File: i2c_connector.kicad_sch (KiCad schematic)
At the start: 5 parts, among them J3 SM04B-SRSS-TB(LF)(SN)

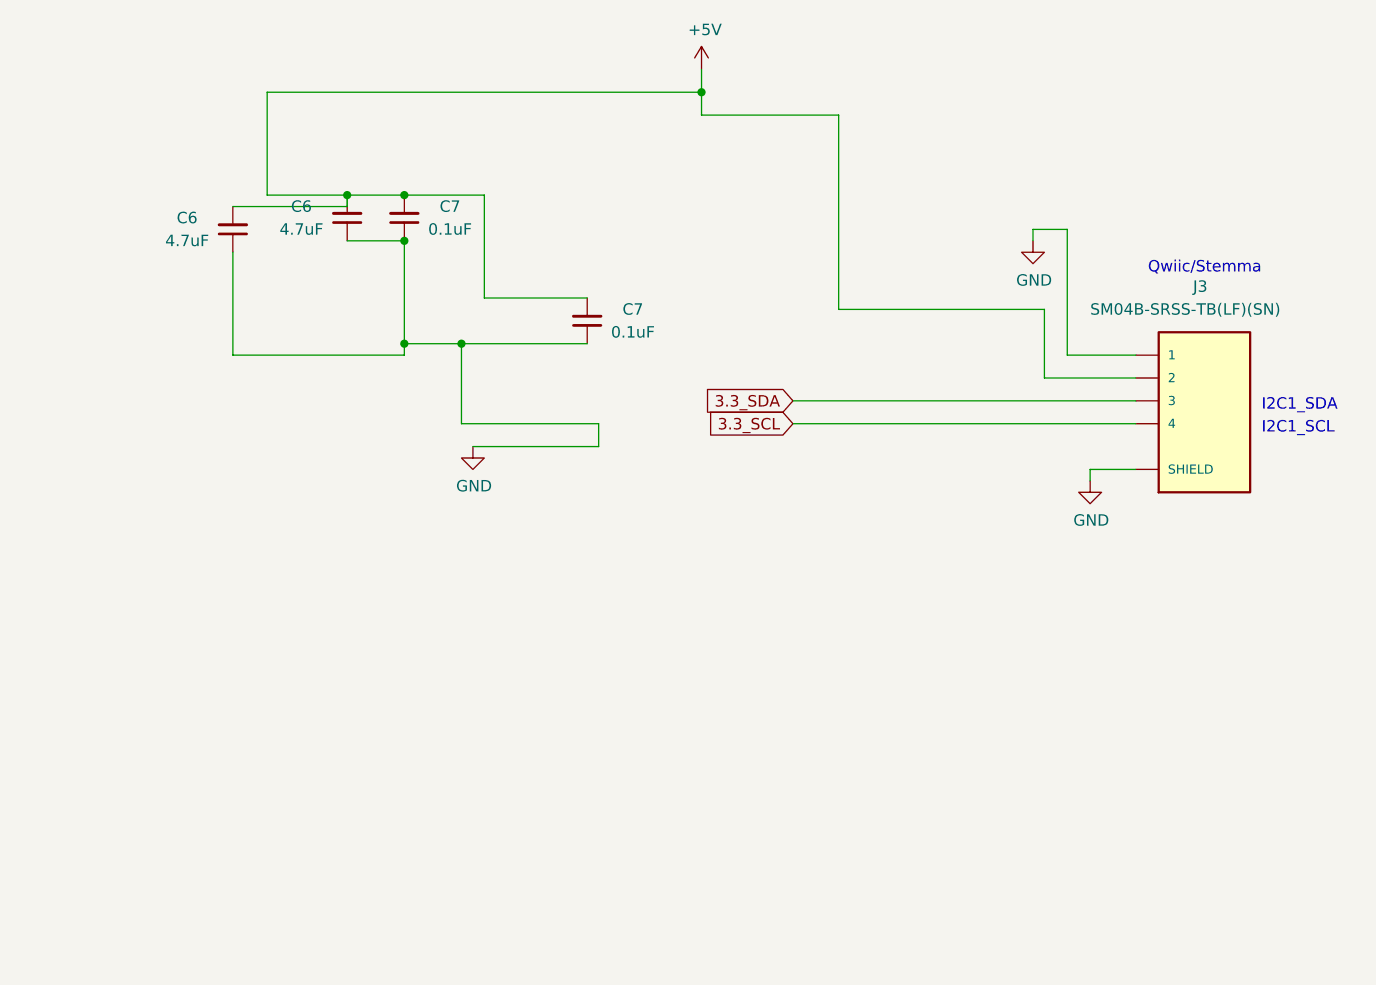
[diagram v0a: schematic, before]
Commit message: Add testpoints
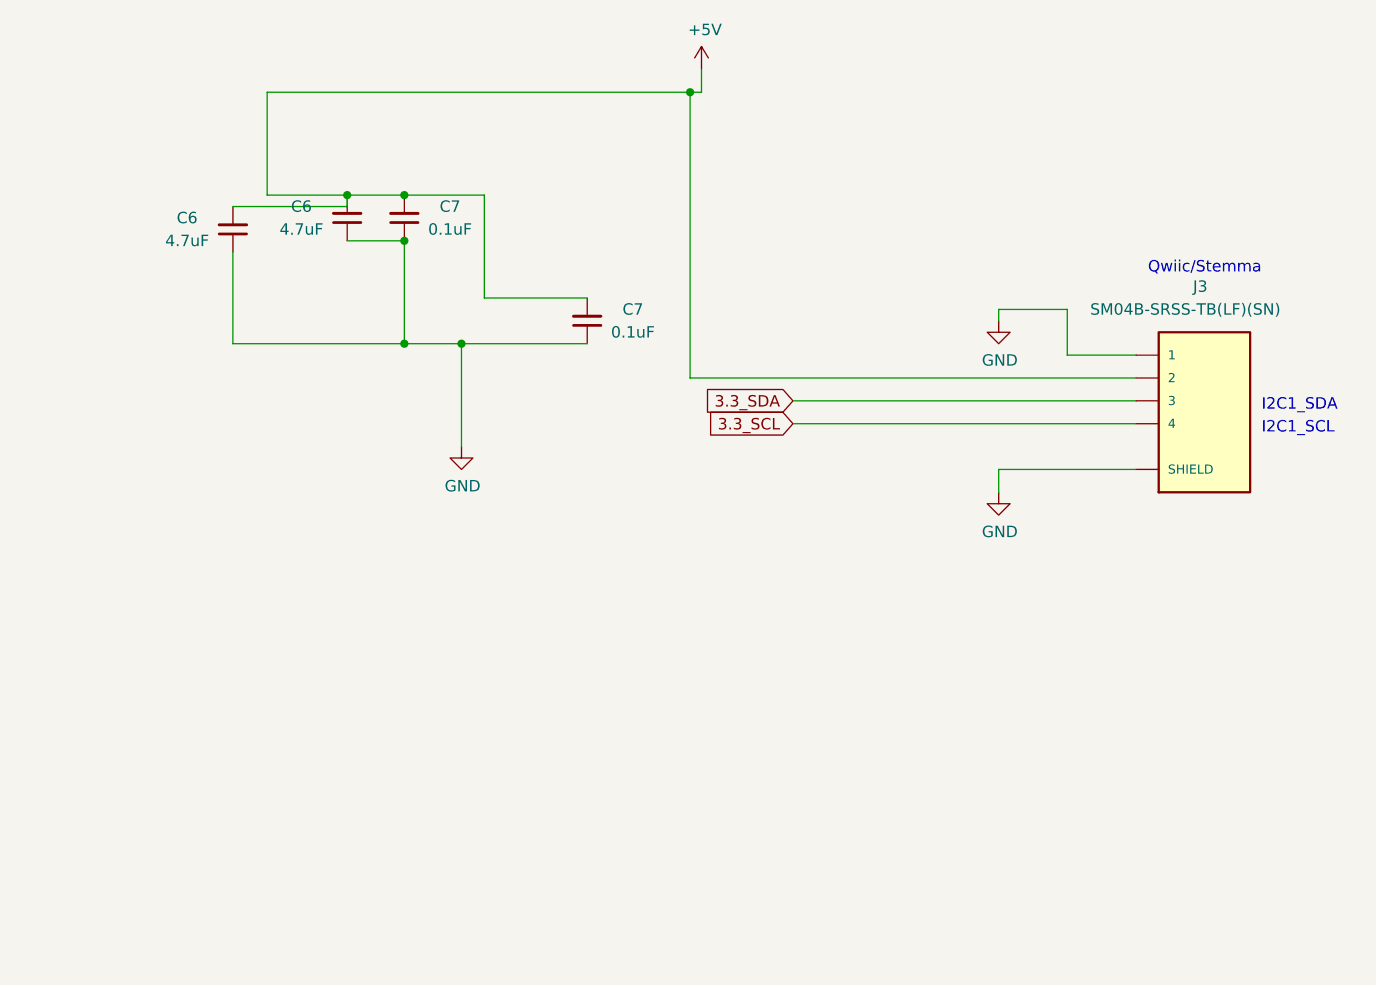
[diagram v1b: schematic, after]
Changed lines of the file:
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@@
   (junction (at 96.52 92.71) (diameter 0) (color 0 0 0 0)
   )
+  (junction (at 128.27 64.77) (diameter 0) (color 0 0 0 0)
+  )
   (junction (at 102.87 92.71) (diameter 0) (color 0 0 0 0)
   )
@@
   (junction (at 90.17 76.2) (diameter 0) (color 0 0 0 0)
   )
-  (junction (at 129.54 64.77) (diameter 0) (color 0 0 0 0)
-  )
-  (wire (pts (xy 172.72 106.68) (xy 172.72 107.95))
-    (stroke (width 0) (type default))
-  )
-  (wire (pts (xy 166.37 81.28) (xy 166.37 80.01))
+  (wire (pts (xy 162.56 106.68) (xy 162.56 109.22))
+    (stroke (width 0) (type default))
+  )
+  (wire (pts (xy 162.56 90.17) (xy 162.56 88.9))
     (stroke (width 0) (type solid))
   )
@@
     (stroke (width 0) (type default))
   )
-  (wire (pts (xy 102.87 92.71) (xy 102.87 101.6))
-    (stroke (width 0) (type default))
-  )
-  (wire (pts (xy 77.47 93.98) (xy 77.47 82.55))
-    (stroke (width 0) (type default))
-  )
-  (wire (pts (xy 96.52 93.98) (xy 96.52 92.71))
-    (stroke (width 0) (type default))
-  )
-  (wire (pts (xy 118.11 101.6) (xy 118.11 104.14))
+  (wire (pts (xy 77.47 92.71) (xy 77.47 82.55))
+    (stroke (width 0) (type default))
+  )
+  (wire (pts (xy 102.87 92.71) (xy 102.87 104.14))
     (stroke (width 0) (type default))
   )
@@
     (stroke (width 0) (type default))
   )
-  (wire (pts (xy 167.64 96.52) (xy 167.64 88.9))
-    (stroke (width 0) (type solid))
-  )
   (wire (pts (xy 139.7 101.6) (xy 177.8 101.6))
     (stroke (width 0) (type solid))
@@
     (stroke (width 0) (type default))
   )
-  (wire (pts (xy 77.47 93.98) (xy 96.52 93.98))
+  (wire (pts (xy 77.47 92.71) (xy 96.52 92.71))
     (stroke (width 0) (type default))
   )
@@
     (stroke (width 0) (type default))
   )
-  (wire (pts (xy 170.18 80.01) (xy 170.18 93.98))
-    (stroke (width 0) (type solid))
-  )
-  (wire (pts (xy 144.78 67.31) (xy 129.54 67.31))
-    (stroke (width 0) (type default))
-  )
-  (wire (pts (xy 102.87 101.6) (xy 118.11 101.6))
+  (wire (pts (xy 170.18 88.9) (xy 170.18 93.98))
+    (stroke (width 0) (type solid))
+  )
+  (wire (pts (xy 128.27 96.52) (xy 177.8 96.52))
     (stroke (width 0) (type default))
   )
@@
     (stroke (width 0) (type default))
   )
-  (wire (pts (xy 118.11 104.14) (xy 104.14 104.14))
-    (stroke (width 0) (type default))
-  )
   (wire (pts (xy 105.41 87.63) (xy 116.84 87.63))
     (stroke (width 0) (type default))
@@
     (stroke (width 0) (type default))
   )
-  (wire (pts (xy 81.28 64.77) (xy 129.54 64.77))
+  (wire (pts (xy 81.28 64.77) (xy 128.27 64.77))
     (stroke (width 0) (type default))
   )
@@
     (stroke (width 0) (type solid))
   )
-  (wire (pts (xy 129.54 64.77) (xy 129.54 67.31))
-    (stroke (width 0) (type default))
-  )
-  (wire (pts (xy 177.8 96.52) (xy 167.64 96.52))
-    (stroke (width 0) (type solid))
-  )
-  (wire (pts (xy 144.78 67.31) (xy 144.78 88.9))
-    (stroke (width 0) (type default))
-  )
-  (wire (pts (xy 177.8 106.68) (xy 172.72 106.68))
+  (wire (pts (xy 128.27 64.77) (xy 129.54 64.77))
+    (stroke (width 0) (type default))
+  )
+  (wire (pts (xy 128.27 64.77) (xy 128.27 96.52))
+    (stroke (width 0) (type default))
+  )
+  (wire (pts (xy 177.8 106.68) (xy 162.56 106.68))
     (stroke (width 0) (type default))
   )
@@
     (stroke (width 0) (type default))
   )
-  (wire (pts (xy 166.37 80.01) (xy 170.18 80.01))
+  (wire (pts (xy 162.56 88.9) (xy 170.18 88.9))
     (stroke (width 0) (type solid))
   )
@@
   )
   (wire (pts (xy 139.7 99.06) (xy 177.8 99.06))
-    (stroke (width 0) (type solid))
-  )
-  (wire (pts (xy 144.78 88.9) (xy 167.64 88.9))
     (stroke (width 0) (type solid))
   )
@@
     )
   )
-  (symbol (lib_id "power:GND") (at 166.37 81.28 0) (unit 1)
-    (in_bom yes) (on_board yes) (dnp no)
-    (property "Reference" "#PWR0109" (at 166.37 87.63 0)
-      (effects (font (size 1.27 1.27)) hide)
-    )
-    (property "Value" "GND" (at 166.497 85.6742 0)
-      (effects (font (size 1.27 1.27)))
-    )
-    (property "Footprint" "" (at 166.37 81.28 0)
-      (effects (font (size 1.27 1.27)) hide)
-    )
-    (property "Datasheet" "" (at 166.37 81.28 0)
+  (symbol (lib_id "power:GND") (at 162.56 90.17 0) (unit 1)
+    (in_bom yes) (on_board yes) (dnp no)
+    (property "Reference" "#PWR0109" (at 162.56 96.52 0)
+      (effects (font (size 1.27 1.27)) hide)
+    )
+    (property "Value" "GND" (at 162.687 94.5642 0)
+      (effects (font (size 1.27 1.27)))
+    )
+    (property "Footprint" "" (at 162.56 90.17 0)
+      (effects (font (size 1.27 1.27)) hide)
+    )
+    (property "Datasheet" "" (at 162.56 90.17 0)
       (effects (font (size 1.27 1.27)) hide)
     )
@@
     )
   )
-  (symbol (lib_id "power:GND") (at 104.14 104.14 0) (unit 1)
-    (in_bom yes) (on_board yes) (dnp no)
-    (property "Reference" "#PWR033" (at 104.14 110.49 0)
-      (effects (font (size 1.27 1.27)) hide)
-    )
-    (property "Value" "GND" (at 104.267 108.5342 0)
-      (effects (font (size 1.27 1.27)))
-    )
-    (property "Footprint" "" (at 104.14 104.14 0)
-      (effects (font (size 1.27 1.27)) hide)
-    )
-    (property "Datasheet" "" (at 104.14 104.14 0)
+  (symbol (lib_id "power:GND") (at 102.87 104.14 0) (unit 1)
+    (in_bom yes) (on_board yes) (dnp no)
+    (property "Reference" "#PWR033" (at 102.87 110.49 0)
+      (effects (font (size 1.27 1.27)) hide)
+    )
+    (property "Value" "GND" (at 102.997 108.5342 0)
+      (effects (font (size 1.27 1.27)))
+    )
+    (property "Footprint" "" (at 102.87 104.14 0)
+      (effects (font (size 1.27 1.27)) hide)
+    )
+    (property "Datasheet" "" (at 102.87 104.14 0)
       (effects (font (size 1.27 1.27)) hide)
     )
@@
     )
   )
-  (symbol (lib_id "power:GND") (at 172.72 107.95 0) (unit 1)
-    (in_bom yes) (on_board yes) (dnp no)
-    (property "Reference" "#PWR0109" (at 172.72 114.3 0)
-      (effects (font (size 1.27 1.27)) hide)
-    )
-    (property "Value" "GND" (at 172.847 112.3442 0)
-      (effects (font (size 1.27 1.27)))
-    )
-    (property "Footprint" "" (at 172.72 107.95 0)
-      (effects (font (size 1.27 1.27)) hide)
-    )
-    (property "Datasheet" "" (at 172.72 107.95 0)
-      (effects (font (size 1.27 1.27)) hide)
-    )
+  (symbol (lib_id "power:GND") (at 162.56 109.22 0) (unit 1)
+    (in_bom yes) (on_board yes) (dnp no)
+    (property "Reference" "#PWR0109" (at 162.56 115.57 0)
+      (effects (font (size 1.27 1.27)) hide)
+    )
+    (property "Value" "GND" (at 162.687 113.6142 0)
+      (effects (font (size 1.27 1.27)))
+    )
+    (property "Footprint" "" (at 162.56 109.22 0)
+      (effects (font (size 1.27 1.27)) hide)
+    )
+    (property "Datasheet" "" (at 162.56 109.22 0)
+      (effects (font (size 1.27 1.27)) hide)
+    )

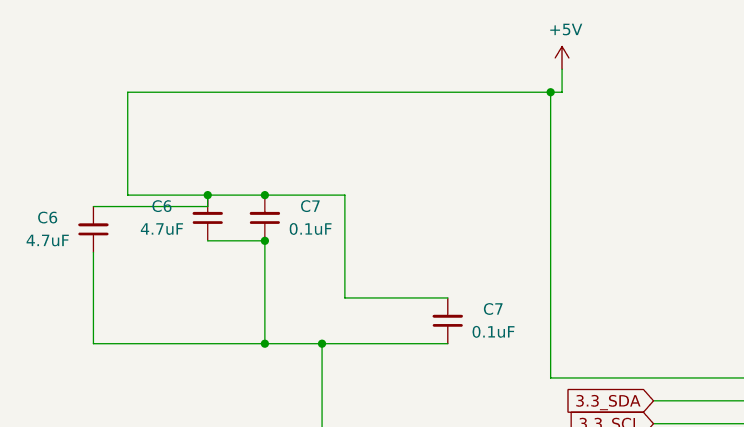
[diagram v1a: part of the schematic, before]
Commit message: Add mcp 2517 can transceiver
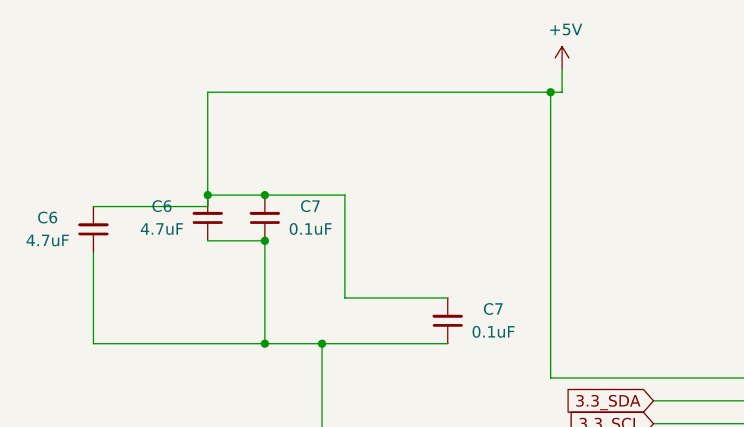
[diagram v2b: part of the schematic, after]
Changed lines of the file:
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@@
     (stroke (width 0) (type solid))
-  )
-  (wire (pts (xy 81.28 76.2) (xy 90.17 76.2))
-    (stroke (width 0) (type default))
   )
   (wire (pts (xy 77.47 92.71) (xy 96.52 92.71))
@@
     (stroke (width 0) (type default))
   )
-  (wire (pts (xy 81.28 76.2) (xy 81.28 64.77))
+  (wire (pts (xy 90.17 76.2) (xy 90.17 64.77))
     (stroke (width 0) (type default))
   )
@@
     (stroke (width 0) (type default))
   )
-  (wire (pts (xy 81.28 64.77) (xy 128.27 64.77))
+  (wire (pts (xy 90.17 64.77) (xy 128.27 64.77))
     (stroke (width 0) (type default))
   )

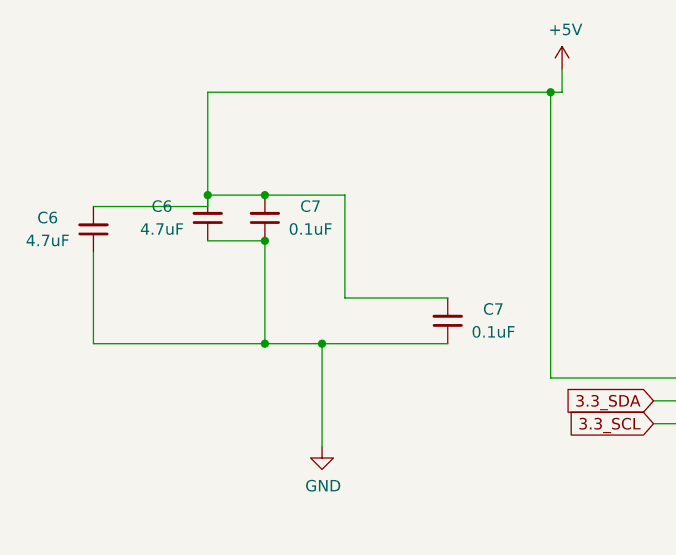
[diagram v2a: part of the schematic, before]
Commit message: Update crystal footprint, move i2c lines to iner layer
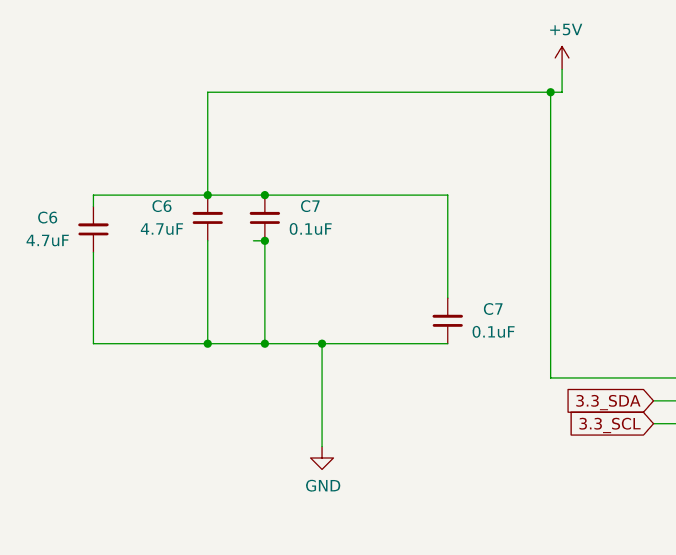
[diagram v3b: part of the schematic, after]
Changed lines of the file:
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@@
   (junction (at 128.27 64.77) (diameter 0) (color 0 0 0 0)
+  )
+  (junction (at 90.17 92.71) (diameter 0) (color 0 0 0 0)
   )
   (junction (at 102.87 92.71) (diameter 0) (color 0 0 0 0)
@@
     (stroke (width 0) (type solid))
   )
-  (wire (pts (xy 90.17 77.47) (xy 90.17 76.2))
+  (wire (pts (xy 77.47 92.71) (xy 77.47 82.55))
     (stroke (width 0) (type default))
   )
-  (wire (pts (xy 77.47 92.71) (xy 77.47 82.55))
+  (wire (pts (xy 116.84 76.2) (xy 116.84 87.63))
     (stroke (width 0) (type default))
   )
@@
     (stroke (width 0) (type default))
   )
-  (wire (pts (xy 77.47 77.47) (xy 90.17 77.47))
+  (wire (pts (xy 90.17 92.71) (xy 90.17 81.28))
     (stroke (width 0) (type default))
   )
@@
     (stroke (width 0) (type solid))
   )
-  (wire (pts (xy 77.47 92.71) (xy 96.52 92.71))
+  (wire (pts (xy 77.47 92.71) (xy 90.17 92.71))
     (stroke (width 0) (type default))
   )
@@
     (stroke (width 0) (type default))
   )
-  (wire (pts (xy 105.41 87.63) (xy 116.84 87.63))
-    (stroke (width 0) (type default))
-  )
   (wire (pts (xy 102.87 92.71) (xy 116.84 92.71))
     (stroke (width 0) (type default))
@@
     (stroke (width 0) (type default))
   )
-  (wire (pts (xy 90.17 81.28) (xy 96.52 81.28))
+  (wire (pts (xy 77.47 76.2) (xy 77.47 77.47))
     (stroke (width 0) (type default))
   )
@@
     (stroke (width 0) (type default))
   )
+  (wire (pts (xy 90.17 92.71) (xy 96.52 92.71))
+    (stroke (width 0) (type default))
+  )
+  (wire (pts (xy 95.25 81.28) (xy 96.52 81.28))
+    (stroke (width 0) (type default))
+  )
   (wire (pts (xy 128.27 64.77) (xy 128.27 96.52))
+    (stroke (width 0) (type default))
+  )
+  (wire (pts (xy 77.47 76.2) (xy 90.17 76.2))
     (stroke (width 0) (type default))
   )
@@
     (stroke (width 0) (type solid))
   )
-  (wire (pts (xy 105.41 87.63) (xy 105.41 76.2))
+  (wire (pts (xy 96.52 76.2) (xy 116.84 76.2))
     (stroke (width 0) (type default))
   )
-  (wire (pts (xy 96.52 76.2) (xy 105.41 76.2))
-    (stroke (width 0) (type default))
-  )

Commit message: Fix connections
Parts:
- removed C6 (x2): 4.7uF, Capacitor_SMD:C_0603_1608Metric, symbol Device:C_Small
- added C11: 10uF, Capacitor_SMD:C_0603_1608Metric, symbol Device:C_Small
- added R3: 10k, Resistor_SMD:R_0603_1608Metric, symbol Device:R
- added R3: 47k, Resistor_SMD:R_0603_1608Metric, symbol Device:R
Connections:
- net +5V: now also C11.1, R3.2, R3.2
- net GND: now also C11.2
- net 3.3_SCL renamed SCL
- net SCL: now also R3.1
- net 3.3_SDA renamed SDA
- net SDA: now also R3.1

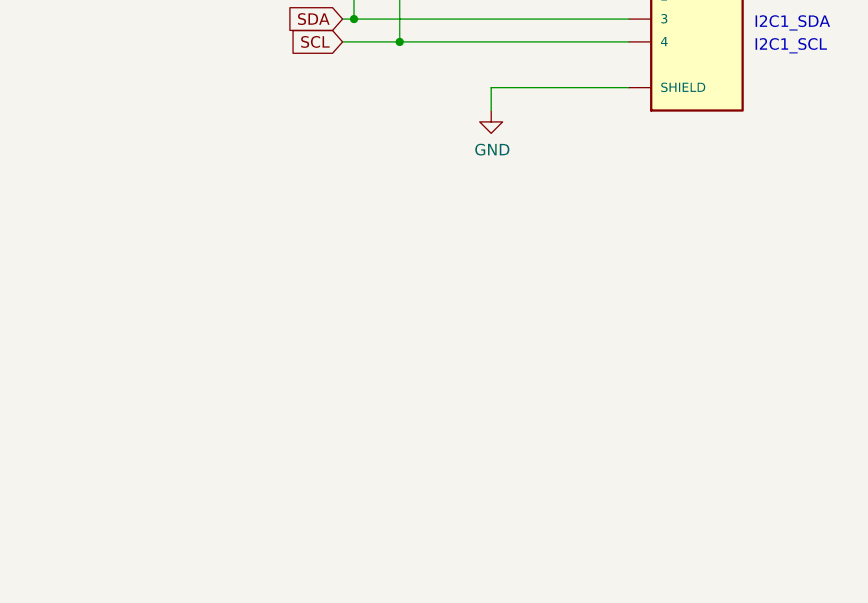
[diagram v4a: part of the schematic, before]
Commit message: Route switches connections
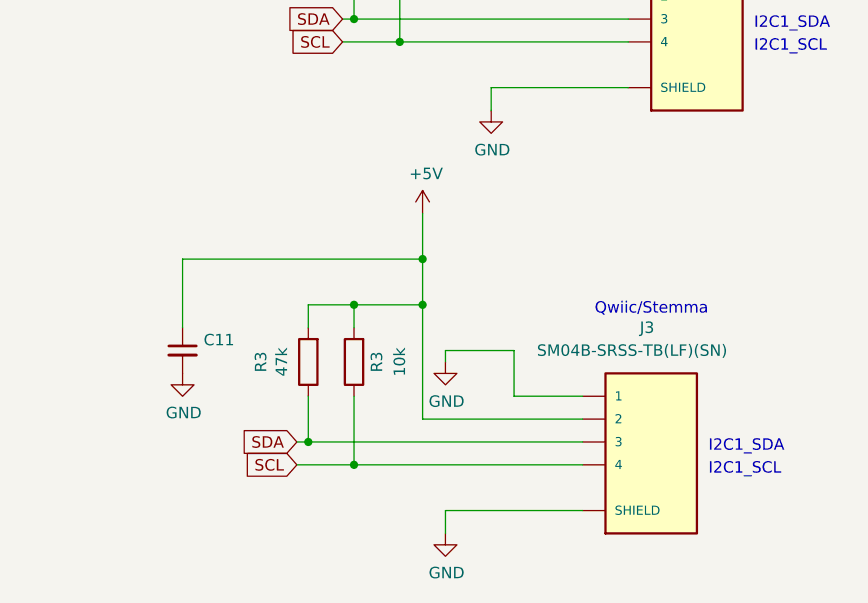
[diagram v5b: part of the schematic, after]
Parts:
- added C11: 10uF, Capacitor_SMD:C_0603_1608Metric, symbol Device:C_Small
- added J3: SM04B-SRSS-TB(LF)(SN), LTP-305G:JST_SM04B-SRSS-TB(LF)(SN), symbol SM04B-SRSS-TB_LF__SN_:SM04B-SRSS-TB(LF)(SN)
- added R3: 10k, Resistor_SMD:R_0603_1608Metric, symbol Device:R
- added R3: 47k, Resistor_SMD:R_0603_1608Metric, symbol Device:R
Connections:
- net +5V: now also C11.1, J3.2, R3.2, R3.2
- net GND: now also C11.2, J3.1, J3.S1 (SHIELD), J3.S2 (SHIELD)
- net SCL: now also J3.4, R3.1
- net SDA: now also J3.3, R3.1
